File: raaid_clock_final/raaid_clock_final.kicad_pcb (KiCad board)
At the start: 2 copper layers, 140 x 90 mm, 59 parts, among them J1 Conn_01x06, J2 Power_inlet_vertical, J3 Conn_02x03_Odd_Even, Q1 NPN_2N3904_SOT23, SW1 Omron_B3F_SPST, SW2 Omron_B3F_SPST, SW3 Omron_B3F_SPST, SW4 Omron_B3F_SPST, SW5 Omron_B3F_SPST, U1 ATmega328-PU, U2 L7805, U3 MAX7219, U4 UltrasonicModule, U5 DS1307_DIP-8, Y1 Crystal_16MHz, Y2 Crystal_32768Hz

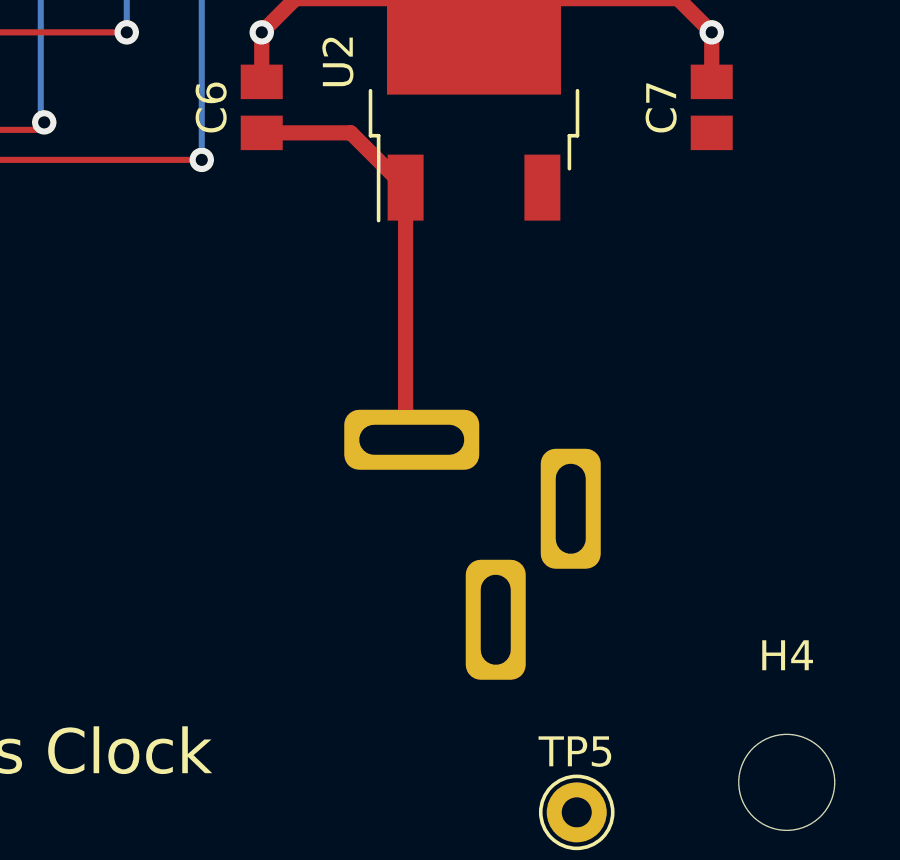
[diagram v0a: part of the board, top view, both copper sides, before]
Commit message: moved inlet; redid gerbers
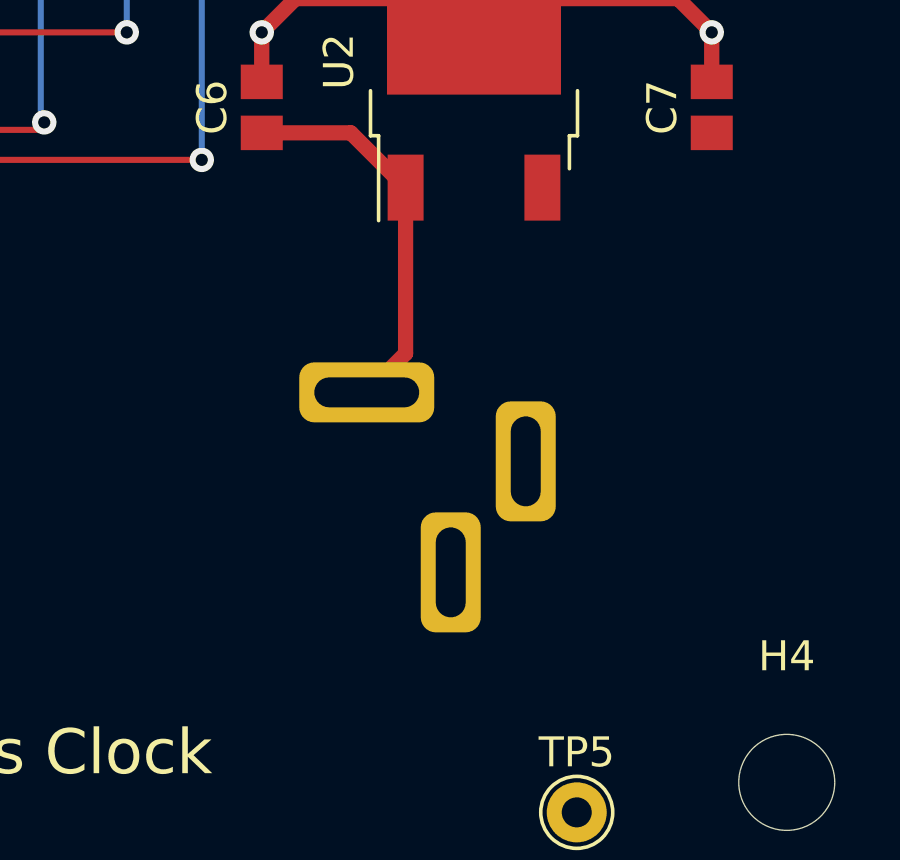
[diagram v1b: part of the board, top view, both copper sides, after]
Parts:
- moved J2 2.18 mm to (201.0, 130.5)
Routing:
- net Net-(C6-Pad1): track 14.3 -> 12.9 mm
